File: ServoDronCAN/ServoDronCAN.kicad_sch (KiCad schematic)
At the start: 55 parts, among them J1 PROG, J2 Вход питания, J4 Измерение, J6 Conn_01x02_Pin, J7 Управление, Q1 2N7002, U1 STM32F103C8T6, U2 XL4016E1, U3 MC33063AD, U4 AMS1117-3.3, U5 CA-IF1042LVS, U6 MCP4921, U7 PC817, Y1 8MHz

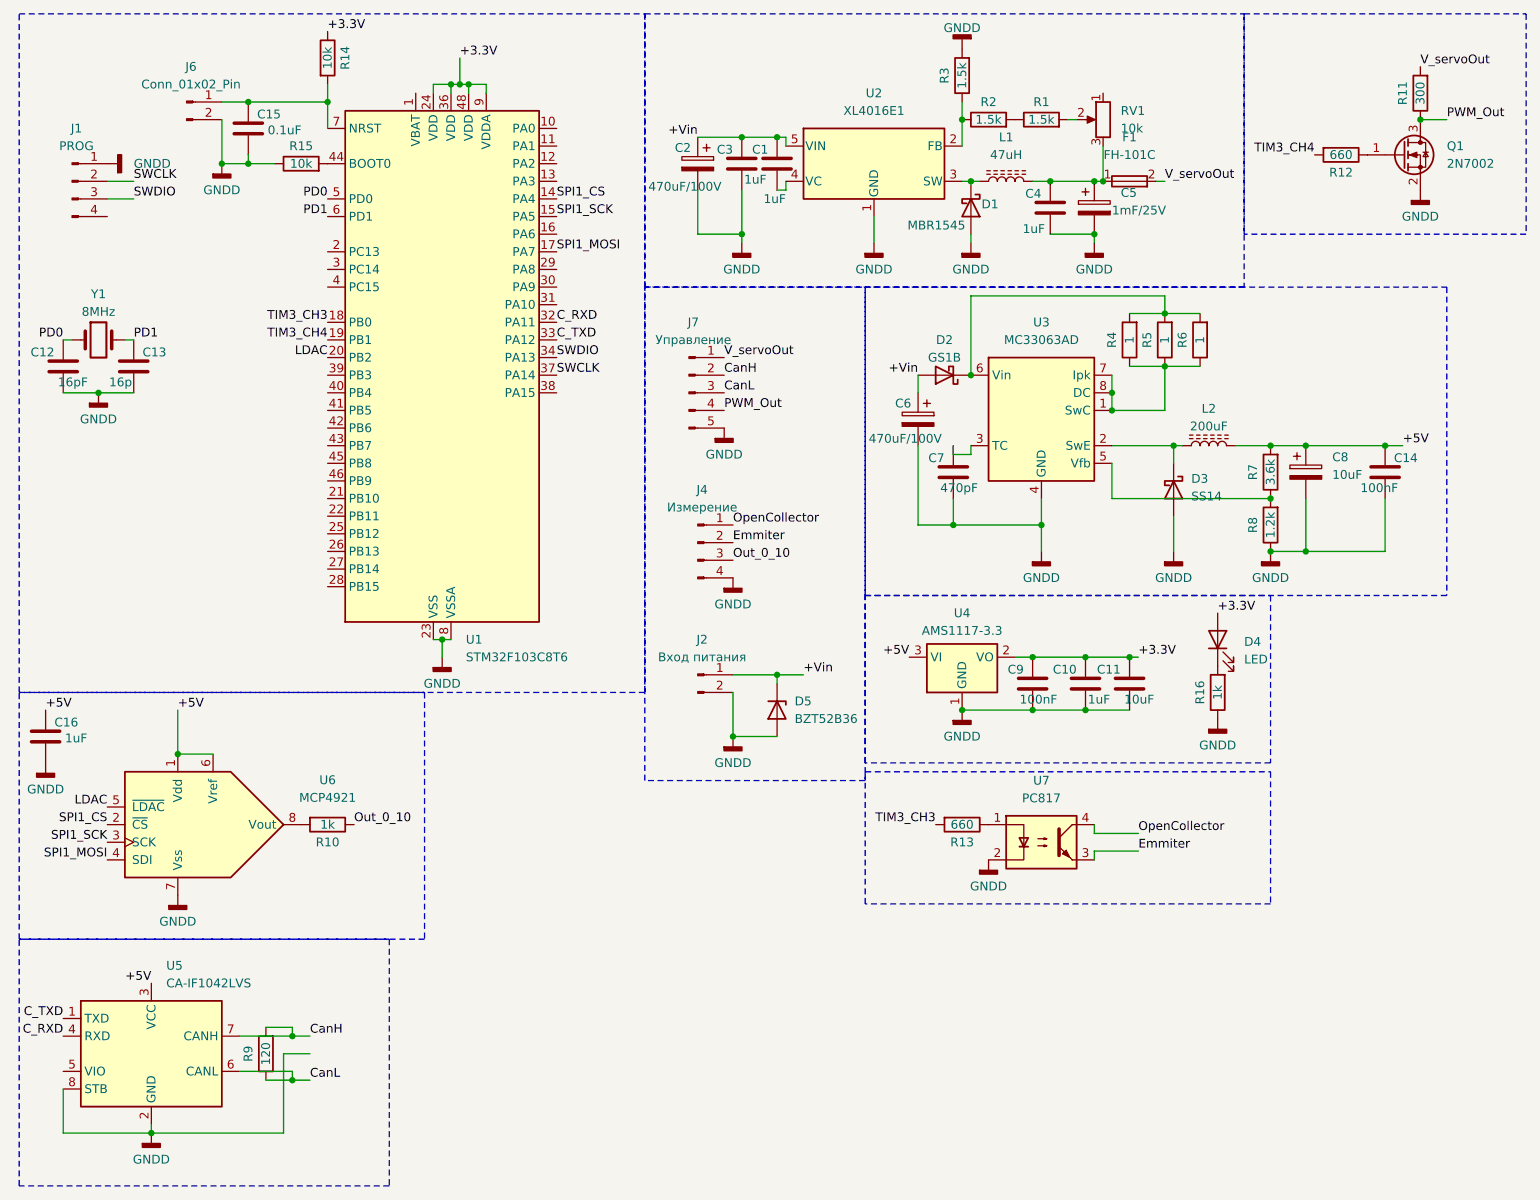
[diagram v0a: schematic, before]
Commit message: Доработана электрическая схема (изменен частотный выход, добавлен разъем для питания вентилтора. Создана печатная плата с расположением компонентов.
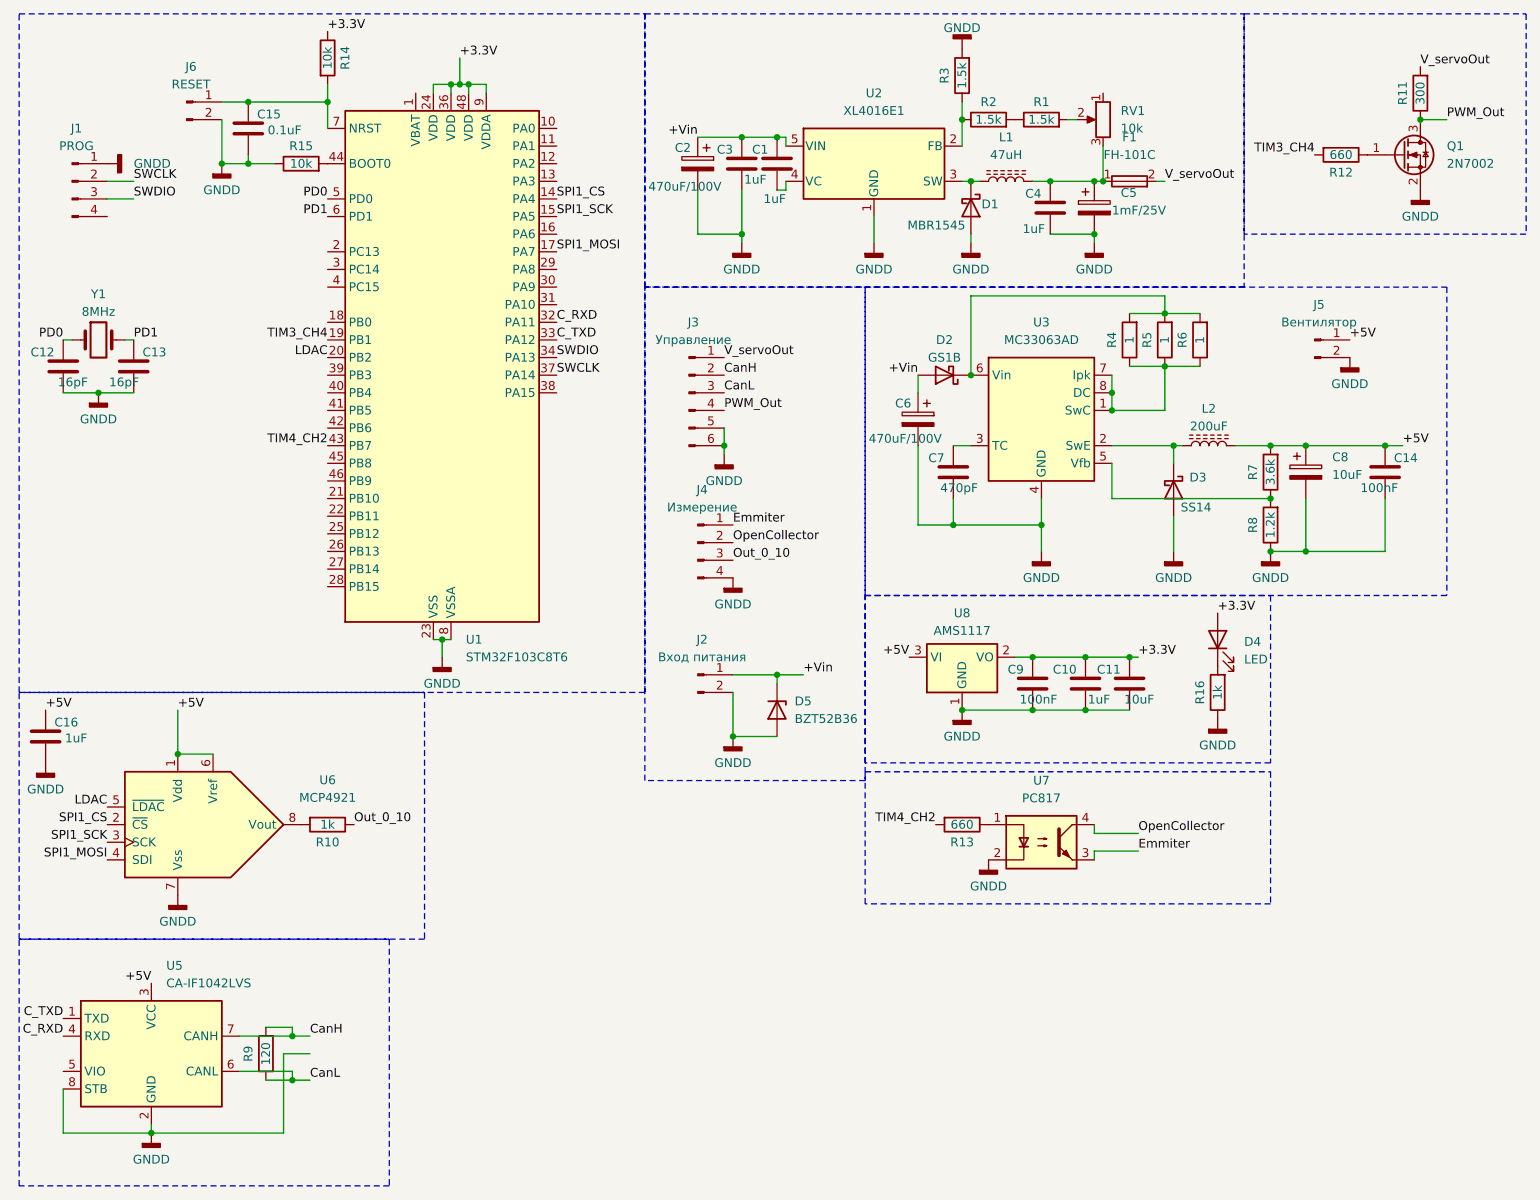
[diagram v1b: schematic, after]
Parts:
- removed J7: Управление, Connector_Phoenix_MC:PhoenixContact_MC_1,5_5-G-3.5_1x05_P3.50mm_Horizontal, symbol Connector:Conn_01x05_Pin
- removed U4: AMS1117-3.3, JLCPCB-Kicad-Footprints:WSON-8_L8.0-W6.0-P1.27-TL-EP-1, symbol Regulator_Linear:AMS1117-3.3
- added J3: Управление, Connector_Phoenix_MC:PhoenixContact_MC_1,5_6-G-3.5_1x06_P3.50mm_Horizontal, symbol Connector:Conn_01x06_Pin
- added J5: Вентилятор, Connector_JST:JST_XH_B2B-XH-A_1x02_P2.50mm_Vertical, symbol Connector:Conn_01x02_Pin
- added U8: AMS1117, Package_TO_SOT_SMD:SOT-223-3_TabPin2, symbol Regulator_Linear:AMS1117
- C13: value 16p -> 16pF
- J6: value Conn_01x02_Pin -> RESET
- RV1: footprint (none) -> Potentiometer_THT:Potentiometer_Bourns_3296W_Vertical
- U1: footprint PCM_JLCPCB:LQFP-48_7x7mm_P0.5mm -> Package_QFP:LQFP-48_7x7mm_P0.5mm
- U2: footprint Package_TO_SOT_THT:TO-220-5_Horizontal_TabDown -> Package_TO_SOT_THT:TO-220-5_P3.4x3.8mm_StaggerOdd_Lead7.13mm_TabDown
- U6: footprint (none) -> Package_SO:SOIC-8_3.9x4.9mm_P1.27mm
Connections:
- net +3.3V: now also U8.2 (VO)
- net +5V: now also J5.1 (Pin_1), U8.3 (VI)
- net CanH: now also J3.2 (Pin_2)
- net CanL: now also J3.3 (Pin_3)
- net Emmiter: now also J4.1 (Pin_1); no longer J4.2 (Pin_2)
- net GNDD: now also J3.5 (Pin_5), J3.6 (Pin_6), J5.2 (Pin_2), U8.1 (GND)
- net OpenCollector: now also J4.2 (Pin_2); no longer J4.1 (Pin_1)
- net PWM_Out: now also J3.4 (Pin_4)
- net V_servoOut: now also J3.1 (Pin_1)
- net TIM4_CH2: now reaches U1.43 (PB7)
- net TIM4_CH2: now also R13.2
- net TIM3_CH3: no longer names the net of U1.18 (PB0)
- net TIM3_CH3: no longer R13.2

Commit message: Исправлена электрическая схема. Добвлена защита от переполюсовки и предохранитель от превышение потребляемоготока (6А). Создан гербер файл для производства.
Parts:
- removed D5: BZT52B36, Diode_SMD:D_SOD-123F, symbol Diode:BZT52Bxx
- removed J5: Вентилятор, Connector_JST:JST_XH_B2B-XH-A_1x02_P2.50mm_Vertical, symbol Connector:Conn_01x02_Pin
- added D6: VS-6CWQ10FNTR-M3, Package_TO_SOT_SMD:TO-252-2, symbol Device:D_Schottky_AAK
- added R17: 18, Resistor_THT:R_Axial_DIN0516_L15.5mm_D5.0mm_P20.32mm_Horizontal, symbol Device:R
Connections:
- net +5V: now also R17.2
- net +Vin: now also F1.2, D6.2 (K); no longer J2.1 (Pin_1)
- net GNDD: now also D6.1 (A), D6.3 (A); no longer J3.5 (Pin_5)
- net V_servoOut: now also C4.1, C5.1, L1.2, RV1.3; no longer F1.2
- new net: F1.1, J2.1 (Pin_1)
- new net: J3.5 (Pin_5), R17.1
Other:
- moved on the sheet: F1
